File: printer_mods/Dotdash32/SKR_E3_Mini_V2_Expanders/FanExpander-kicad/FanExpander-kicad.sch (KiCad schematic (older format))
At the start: 52 parts, among them J1 FAN1_IN, J10 FAN2, J11 V_SELECT3, J12 V_SELECT4, J13 FAN3, J14 FAN4, J15 V_SELECT5, J16 V_SELECT6, J17 FAN5, J18 FAN6, J2 HV_IN, J3 EXP1_IN, J4 TH2, J5 3V3_IN, J6 V_SELECT1, J7 V_SELECT2, J8 TH2, J9 FAN1, Q1 IRLML6344, Q2 IRLML6344, Q3 IRLML6344, Q4 IRLML6344, Q5 IRLML6344

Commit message: feat: no ADC in EXP1, add more fans!!!
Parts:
- removed C1, C2: 10uF, Capacitors_SMD:C_0805, symbol Device:C
- removed J4, J8: TH2, Connectors_JST:JST_XH_B02B-XH-A_02x2.50mm_Straight, symbol Connector_Generic:Conn_01x02
- removed J5: 3V3_IN, Pin_Headers:Pin_Header_Straight_1x01_Pitch2.54mm, symbol Connector_Generic:Conn_01x01
- removed R1, R4: 4.7k, Resistors_SMD:R_0603_HandSoldering, symbol Device:R_US
- added D? (x2): LED, LEDs:LED_0603_HandSoldering, symbol Device:LED
- added J?: FAN7, Connectors_JST:JST_XH_B02B-XH-A_02x2.50mm_Straight, symbol Connector_Generic:Conn_01x02
- added J?: V_SELECT7, Pin_Headers:Pin_Header_Straight_1x03_Pitch2.54mm, symbol Jumper:Jumper_3_Open
- added J?: FAN6, Connectors_JST:JST_XH_B02B-XH-A_02x2.50mm_Straight, symbol Connector_Generic:Conn_01x02
- added J?: V_SELECT8, Pin_Headers:Pin_Header_Straight_1x03_Pitch2.54mm, symbol Jumper:Jumper_3_Open
- added JP1: FAN_SEL, Jumper:SolderJumper-3_P1.3mm_Open_RoundedPad1.0x1.5mm_NumberLabels, symbol Jumper:SolderJumper_3_Open
- added JP2: LED_ENABLE, symbol Jumper:SolderJumper_2_Bridged
- added Q? (x2): IRLML6344, TO_SOT_Packages_SMD:SOT-23, symbol Device:Q_NMOS_GSD
- added R? (x2): 560R, Resistors_SMD:R_0603_HandSoldering, symbol Device:R_US
- added R? (x2): 100R, Resistors_SMD:R_0603_HandSoldering, symbol Device:R_US
- added R? (x2): 100k, Resistors_SMD:R_0603_HandSoldering, symbol Device:R_US
- J11, J12, J15, J16, J6, J7: symbol Connector_Generic:Conn_01x03 -> Jumper:Jumper_3_Open
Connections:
- net TH2 is gone; now on net FAN3: J3.3 (Pin_3)
- net TH3 is gone; now on net FAN4: J3.5 (Pin_5)
- net +24V: now also J?.3 (B), J?.3 (B)
- net +5V: now also J?.1 (A), J?.1 (A), JP2.1 (A); no longer R13.2, R14.2, R2.2, R3.2, R7.2, R8.2
- net F6V: now also J?.1 (Pin_1), J?.1 (Pin_1), J?.2 (C), J?.2 (C)
- net FAN3: now also R9.2; no longer J3.7 (Pin_7), R9.1
- net FAN4: now also R10.2; no longer J3.2 (Pin_2), R10.1
- net FAN5: now also J3.7 (Pin_7), R15.2; no longer J3.6 (Pin_6), R15.1
- net FAN6: now also J3.2 (Pin_2); no longer J3.8 (Pin_8)
- net GND: now also R10.1, R15.1, R9.1, Q?.2 (S), Q?.2 (S), R?.2, R?.2; no longer R10.2, R15.2, R9.2
- net at J3.4 (Pin_4): now also JP1.3 (B)
- net toFuse24V: no longer names the net of F1.2
- net toFuse24V: no longer J1.1 (Pin_1)
- net toFuse5V: no longer names the net of F3.2
- net toFuse5V: no longer J3.10 (Pin_10)
- new net: J3.8 (Pin_8), JP1.1 (A)
- new net: Q?.1 (G), R?.1 (x2)
- new net: D?.2 (A), R?.1 (x2)
- new net 24V_unFused: J1.1 (Pin_1)
- new net 5V_unFused: J3.10 (Pin_10)
- new net FAN7: J3.6 (Pin_6), R?.1, R?.2
- new net FAN7_Drive: D?.1 (K), J?.2 (Pin_2), Q?.3 (D)
- new net FAN8: JP1.2 (C), R?.1, R?.2
- new net FAN8_Drive: D?.1 (K), J?.2 (Pin_2), Q?.3 (D)
- new net LED_Drive: JP2.2 (B), R13.2, R14.2, R2.2, R3.2, R7.2, R8.2, R?.2, R?.2
- no-connect marks 1 -> 0
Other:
- note added: "FAN1"
- note added: "FAN1 is a pass through fan.\nIt is included for a simple +12/24V reference,\nand to select drive voltage.\n\nNo control is done to this fan!"
- note added: "FAN1\nfrom SKR"
- note added: "Fan2"
- note added: "Fan3"
- note added: "Fan4"
- note added: "Fan5"
- note added: "Fan6"
- note added: "Fan7"
- note added: "Fan8"
- note added: "SKR Mini E3 V2.0\nPB5 | PA15\nTX1/PA9 | RST\nRX1/PA10 | PB9\nPB8 | PB15\nGND | +5V"
- note removed: "3.3V \nfrom SKR"
- note removed: "FAN1 - Passthrough"
- note removed: "FAN1 from SKR"
- note removed: "Fan2 - PB5"
- note removed: "Fan3 - PB8"
- note removed: "Fan4 - PA15"
- note removed: "Fan5 - PB9"
- note removed: "Fan6 - PB15"
- note removed: "PB5 | PA15\nTX1/PA9 | RST\nRX1/PA10 | PB9\nPB8 | PB15\nGND | +5V"
- note removed: "TH2 - PA9"
- note removed: "TH3 - PA10"
- note removed: "Thermistor Inputs"
- moved on the sheet: D3, D4, D5, D6, D7, D8, F1, F3, J1, J10, J13, J14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

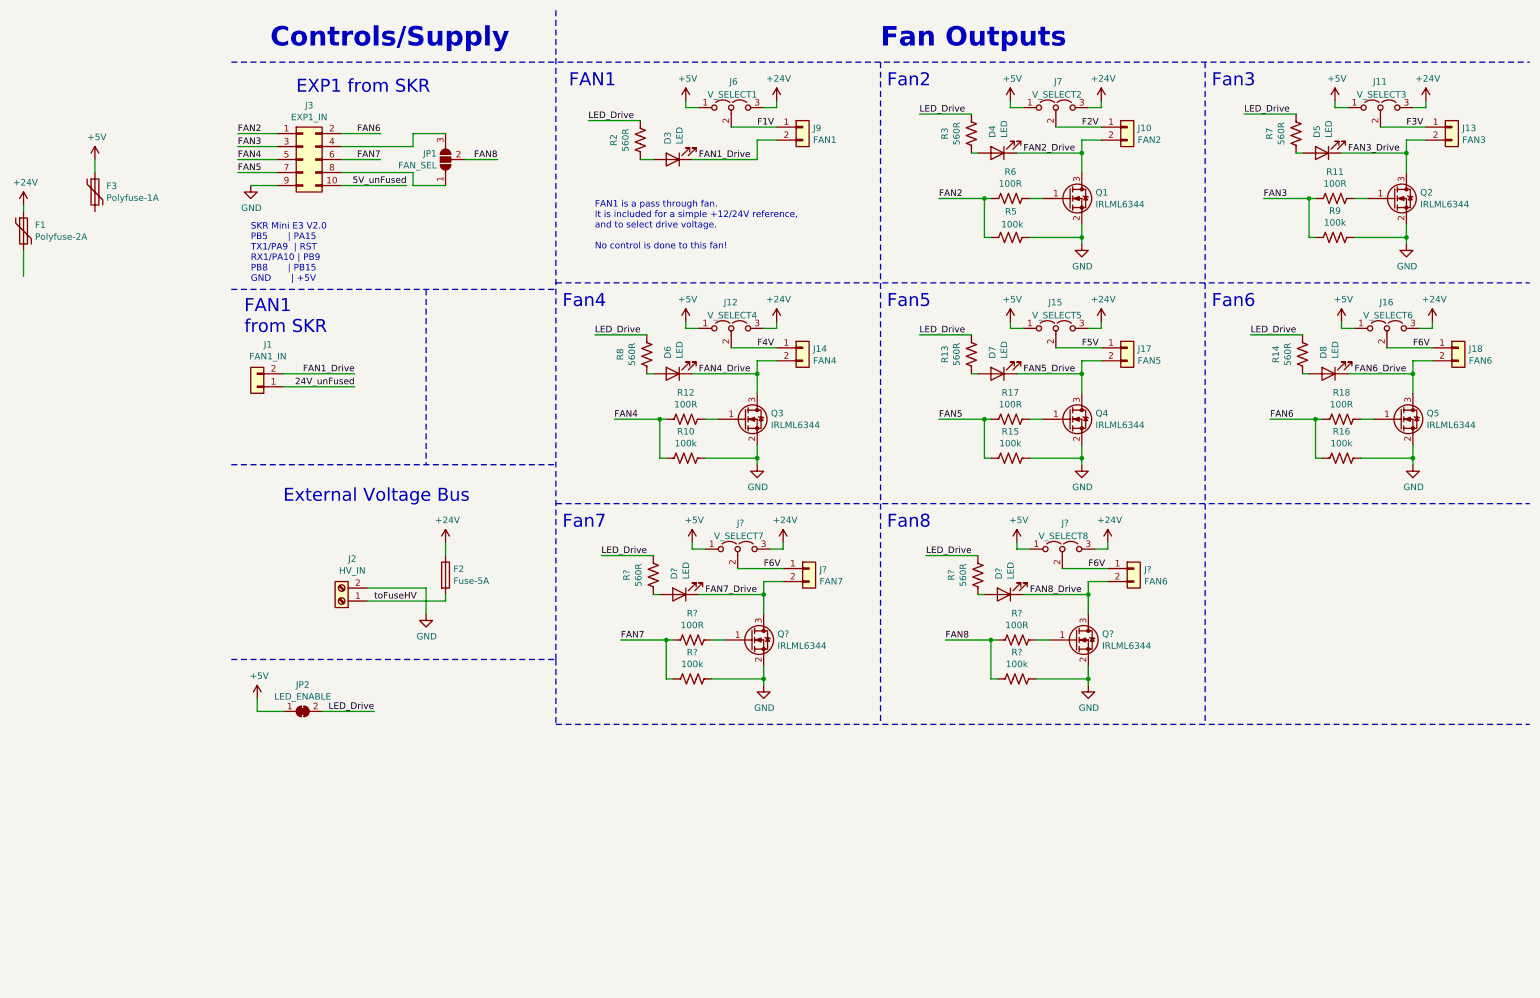
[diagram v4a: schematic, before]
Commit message: feat: beefy expander sch cleaned, initial layout
schematic looks good, but the layout needs work.
RN, it covers too much, so needs to have the EXP header stick out
a lot more than it already is, probably make the whole thing longer
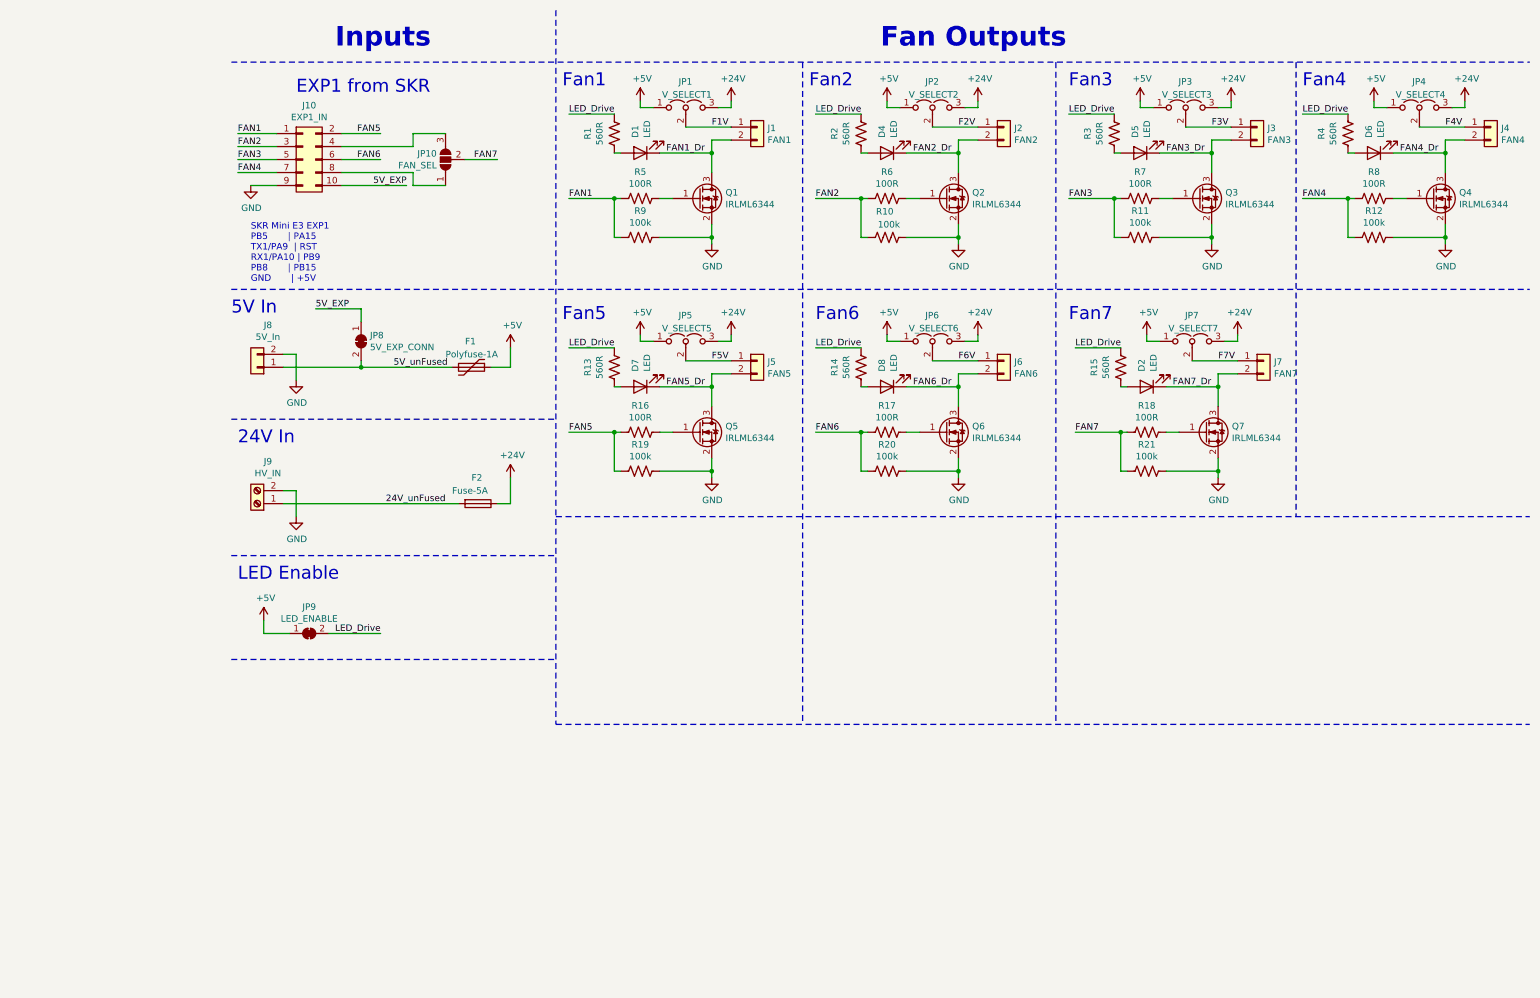
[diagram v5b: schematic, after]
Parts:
- removed D3: LED, LEDs:LED_0603_HandSoldering, symbol Device:LED
- removed F1: Polyfuse-2A, Fuse_Holders_and_Fuses:Fuse_SMD1206_HandSoldering, symbol Device:Polyfuse
- removed J6: V_SELECT1, Pin_Headers:Pin_Header_Straight_1x03_Pitch2.54mm, symbol Jumper:Jumper_3_Open
- removed J9: FAN1, Connectors_JST:JST_XH_B02B-XH-A_02x2.50mm_Straight, symbol Connector_Generic:Conn_01x02
- removed R2: 560R, Resistors_SMD:R_0603_HandSoldering, symbol Device:R_US
- added JP8: 5V_EXP_CONN, Jumper:SolderJumper-2_P1.3mm_Bridged_RoundedPad1.0x1.5mm, symbol Jumper:SolderJumper_2_Bridged
- F2: footprint Fuse_Holders_and_Fuses:BladeFuse-CarType -> Fuse_Holders_and_Fuses:BladeFuse-Mini
- J1: renamed from J?; value FAN6 -> FAN1
- J8: renamed from J1; value FAN1_IN -> 5V_In
- JP1: renamed from J?; value V_SELECT8 -> V_SELECT1
- JP9: renamed from JP2; footprint (none) -> Jumper:SolderJumper-2_P1.3mm_Bridged_RoundedPad1.0x1.5mm
- gave numbers to parts that had none: 12
- renumbered F3 to F1, J3 to J10, J10 to J2, J13 to J3, J14 to J4, J17 to J5, J18 to J6, J2 to J9, JP1 to JP10, J7 to JP2, J11 to JP3, J12 to JP4, J15 to JP5, J16 to JP6, Q1 to Q2, Q2 to Q3, Q3 to Q4, Q4 to Q5, Q5 to Q6, R5 to R10, R9 to R11, R10 to R12, R17 to R16, R18 to R17, R15 to R19, R3 to R2, R16 to R20, R7 to R3, R8 to R4, R11 to R7, R12 to R8
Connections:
- net FAN1_Drive is gone; now on net GND: J8.2 (Pin_2)
- net toFuseHV is gone; now on net 24V_unFused: F2.2, J9.1 (Pin_1)
- net 24V_unFused: no longer J8.1 (Pin_1)
- net 5V_unFused: now also F1.2, J8.1 (Pin_1), JP8.2 (B); no longer J10.10 (Pin_10)
- net F1V: now also J1.1 (Pin_1), JP1.2 (C)
- net F6V: no longer J1.1 (Pin_1), J7.1 (Pin_1), JP1.2 (C), JP7.2 (C)
- net FAN2: now also J10.3 (Pin_3); no longer J10.1 (Pin_1)
- net FAN3: now also J10.5 (Pin_5); no longer J10.3 (Pin_3)
- net FAN4: now also J10.7 (Pin_7); no longer J10.5 (Pin_5)
- net FAN5: now also J10.2 (Pin_2); no longer J10.7 (Pin_7)
- net FAN6: now also J10.6 (Pin_6); no longer J10.2 (Pin_2)
- net FAN7: now also JP10.2 (C); no longer J10.6 (Pin_6)
- net FAN2_Drive renamed FAN2_Dr
- net FAN3_Drive renamed FAN3_Dr
- net FAN4_Drive renamed FAN4_Dr
- net FAN5_Drive renamed FAN5_Dr
- net FAN6_Drive renamed FAN6_Dr
- net FAN7_Drive renamed FAN7_Dr
- net FAN8 renamed FAN1
- net FAN1: now also J10.1 (Pin_1); no longer JP10.2 (C)
- net FAN8_Drive renamed FAN1_Dr
- new net 5V_EXP: J10.10 (Pin_10), JP8.1 (A)
- new net F7V: J7.1 (Pin_1), JP7.2 (C)
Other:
- note added: "24V In"
- note added: "5V In"
- note added: "Fan1"
- note added: "Inputs"
- note added: "LED Enable"
- note added: "SKR Mini E3 EXP1\nPB5 | PA15\nTX1/PA9 | RST\nRX1/PA10 | PB9\nPB8 | PB15\nGND | +5V"
- note removed: "Controls/Supply"
- note removed: "External Voltage Bus"
- note removed: "FAN1"
- note removed: "FAN1 is a pass through fan.\nIt is included for a simple +12/24V reference,\nand to select drive voltage.\n\nNo control is done to this fan!"
- note removed: "FAN1\nfrom SKR"
- note removed: "Fan8"
- note removed: "SKR Mini E3 V2.0\nPB5 | PA15\nTX1/PA9 | RST\nRX1/PA10 | PB9\nPB8 | PB15\nGND | +5V"
- moved on the sheet: D1, D2, D4, D5, D6, D7, D8, F1, F2, J1, J2, J3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

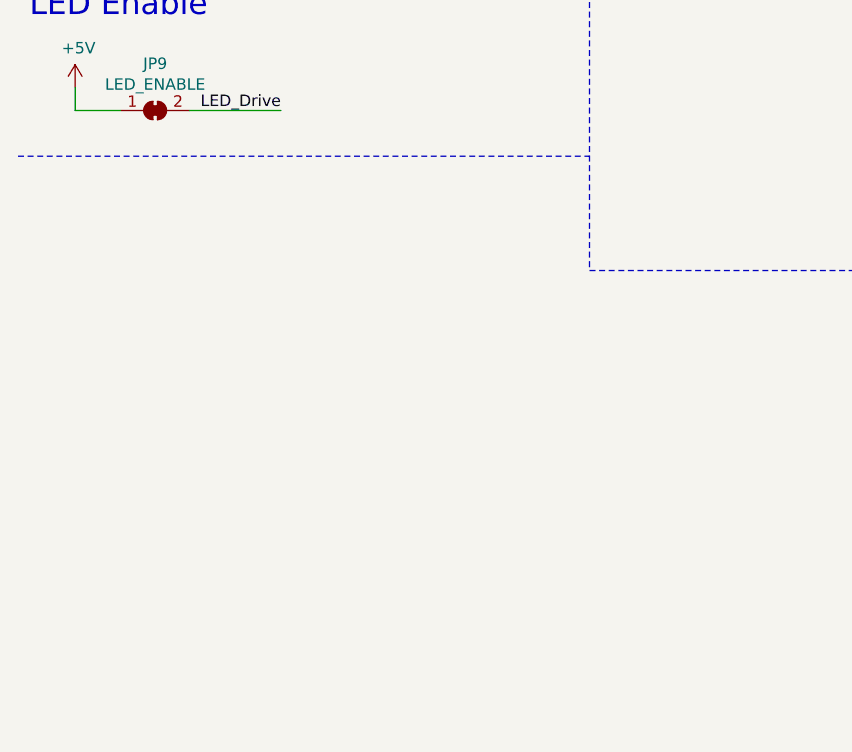
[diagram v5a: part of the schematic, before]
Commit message: test: using 1xXX pins for breakaways?
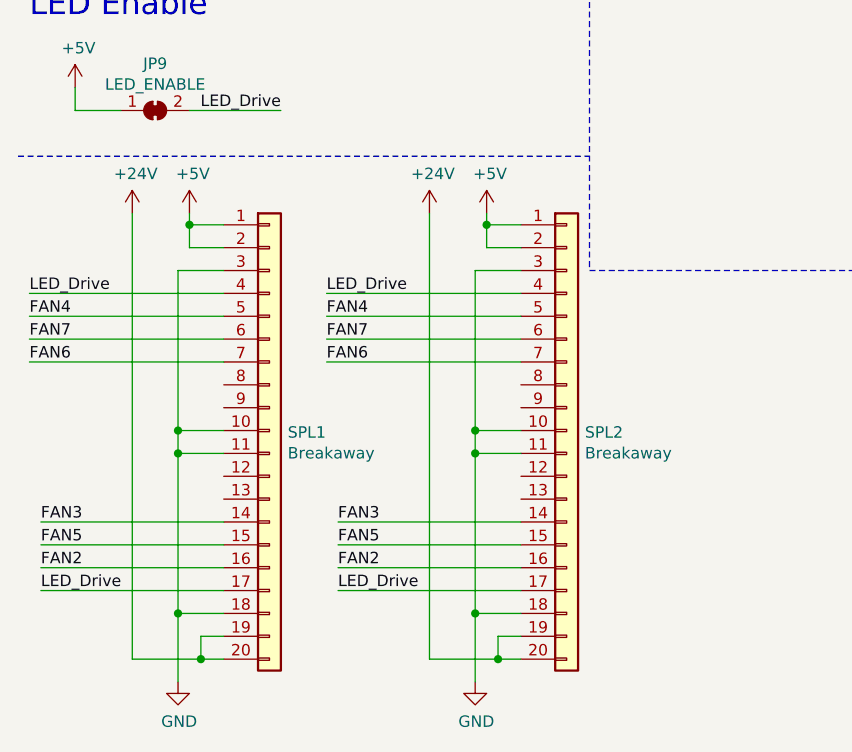
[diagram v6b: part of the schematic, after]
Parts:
- added SPL1, SPL2: Breakaway, Pin_Headers:Pin_Header_Straight_1x20_Pitch1.00mm, symbol Connector_Generic:Conn_01x20
- F1: footprint Fuse_Holders_and_Fuses:Fuse_SMD1206_HandSoldering -> Fuse_Holders_and_Fuses:Fuse_SMD1206_Reflow
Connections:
- net +24V: now also SPL1.19 (Pin_19), SPL1.20 (Pin_20), SPL2.19 (Pin_19), SPL2.20 (Pin_20)
- net +5V: now also SPL1.1 (Pin_1), SPL1.2 (Pin_2), SPL2.1 (Pin_1), SPL2.2 (Pin_2)
- net FAN2: now also SPL1.16 (Pin_16), SPL2.16 (Pin_16)
- net FAN3: now also SPL1.14 (Pin_14), SPL2.14 (Pin_14)
- net FAN4: now also SPL1.5 (Pin_5), SPL2.5 (Pin_5)
- net FAN5: now also SPL1.15 (Pin_15), SPL2.15 (Pin_15)
- net FAN6: now also SPL1.7 (Pin_7), SPL2.7 (Pin_7)
- net FAN7: now also SPL1.6 (Pin_6), SPL2.6 (Pin_6)
- net GND: now also SPL1.10 (Pin_10), SPL1.11 (Pin_11), SPL1.18 (Pin_18), SPL1.3 (Pin_3), SPL2.10 (Pin_10), SPL2.11 (Pin_11), SPL2.18 (Pin_18), SPL2.3 (Pin_3)
- net LED_Drive: now also SPL1.17 (Pin_17), SPL1.4 (Pin_4), SPL2.17 (Pin_17), SPL2.4 (Pin_4)
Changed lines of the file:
@@
 F 0 "F1" V 2150 3200 50  0000 L CNN
 F 1 "Polyfuse-1A" V 2250 3050 50  0000 L CNN
-F 2 "Fuse_Holders_and_Fuses:Fuse_SMD1206_HandSoldering" H 2400 3050 50  0001 L CNN
+F 2 "Fuse_Holders_and_Fuses:Fuse_SMD1206_Reflow" H 2400 3050 50  0001 L CNN
 F 3 "~" H 2350 3250 50  0001 C CNN
 	1    2350 3250
@@
 Text Notes 550  4900 0    100  ~ 0
 LED Enable
-Wire Notes Line
-	500  5500 3000 5500
 Wire Notes Line width 12 style solid
 	3000 500  3000 6000
@@
 Wire Wire Line
 	1500 3250 2200 3250
+$Comp
+L power:GND #PWR0103
+U 1 1 61E47425
+P 1200 7800
+F 0 "#PWR0103" H 1200 7550 50  0001 C CNN
+F 1 "GND" H 1205 7627 50  0000 C CNN
+F 2 "" H 1200 7800 50  0001 C CNN
+F 3 "" H 1200 7800 50  0001 C CNN
+	1    1200 7800
+	1    0    0    -1
+$EndComp
+$Comp
+L Connector_Generic:Conn_01x20 SPL1
+U 1 1 61ED7192
+P 1600 6700
+F 0 "SPL1" H 1680 6692 50  0000 L CNN
+F 1 "Breakaway" H 1680 6601 50  0000 L CNN
+F 2 "Pin_Headers:Pin_Header_Straight_1x20_Pitch1.00mm" H 1600 6700 50  0001 C CNN
+F 3 "~" H 1600 6700 50  0001 C CNN
+	1    1600 6700
+	1    0    0    -1
+$EndComp
+$Comp
+L power:+24V #PWR0105
+U 1 1 61EDE44B
+P 1000 5750
+F 0 "#PWR0105" H 1000 5600 50  0001 C CNN
+F 1 "+24V" H 1015 5923 50  0000 C CNN
+F 2 "" H 1000 5750 50  0001 C CNN
+F 3 "" H 1000 5750 50  0001 C CNN
+	1    1000 5750
+	1    0    0    -1
+$EndComp
+$Comp
+L power:+5V #PWR0106
+U 1 1 61EDCDF9
+P 1250 5750
+F 0 "#PWR0106" H 1250 5600 50  0001 C CNN
+F 1 "+5V" H 1265 5923 50  0000 C CNN
+F 2 "" H 1250 5750 50  0001 C CNN
+F 3 "" H 1250 5750 50  0001 C CNN
+	1    1250 5750
+	1    0    0    -1
+$EndComp
+Wire Wire Line
+	1250 5750 1250 5800
+Wire Wire Line
+	1250 5800 1400 5800
+Wire Wire Line
+	1400 5900 1250 5900
+Wire Wire Line
+	1250 5900 1250 5800
+Connection ~ 1250 5800
+Wire Wire Line
+	1000 5750 1000 7700
+Wire Wire Line
+	1000 7700 1300 7700
+Wire Wire Line
+	1400 7600 1300 7600
+Wire Wire Line
+	1300 7600 1300 7700
+Connection ~ 1300 7700
+Wire Wire Line
+	1300 7700 1400 7700
+Wire Wire Line
+	1200 7800 1200 7500
+Wire Wire Line
+	1200 7500 1400 7500
+Wire Wire Line
+	1200 7500 1200 6800
+Wire Wire Line
+	1200 6000 1400 6000
+Connection ~ 1200 7500
+Wire Wire Line
+	1400 6100 550  6100
+Text Label 550  6100 0    50   ~ 0
+LED_Drive
+Wire Wire Line
+	1400 6700 1200 6700
+Connection ~ 1200 6700
+Wire Wire Line
+	1200 6700 1200 6000
+Wire Wire Line
+	1400 6800 1200 6800
+Connection ~ 1200 6800
+Wire Wire Line
+	1200 6800 1200 6700
+Wire Wire Line
+	1400 6200 550  6200
+Wire Wire Line
+	1400 6300 550  6300
+Wire Wire Line
+	1400 6400 550  6400
+Wire Wire Line
+	1400 7400 600  7400
+Wire Wire Line
+	1400 7300 600  7300
+Wire Wire Line
+	1400 7200 600  7200
+Wire Wire Line
+	1400 7100 600  7100
+Text Label 600  7300 0    50   ~ 0
+FAN2
+Text Label 600  7200 0    50   ~ 0
+FAN5
+Text Label 550  6200 0    50   ~ 0
+FAN4
+Text Label 550  6300 0    50   ~ 0
+FAN7
+Text Label 600  7100 0    50   ~ 0
+FAN3
+Text Label 550  6400 0    50   ~ 0
+FAN6
+Text Label 600  7400 0    50   ~ 0
+LED_Drive
+$Comp
+L power:GND #PWR0107
+U 1 1 61FFF90D
+P 2500 7800
+F 0 "#PWR0107" H 2500 7550 50  0001 C CNN
+F 1 "GND" H 2505 7627 50  0000 C CNN
+F 2 "" H 2500 7800 50  0001 C CNN
+F 3 "" H 2500 7800 50  0001 C CNN
+	1    2500 7800
+	1    0    0    -1
+$EndComp
+$Comp
+L Connector_Generic:Conn_01x20 SPL2
+U 1 1 61FFF913
+P 2900 6700
+F 0 "SPL2" H 2980 6692 50  0000 L CNN
+F 1 "Breakaway" H 2980 6601 50  0000 L CNN
+F 2 "Pin_Headers:Pin_Header_Straight_1x20_Pitch1.00mm" H 2900 6700 50  0001 C CNN
+F 3 "~" H 2900 6700 50  0001 C CNN
+	1    2900 6700
+	1    0    0    -1
+$EndComp
+$Comp
+L power:+24V #PWR0108
+U 1 1 61FFF919
+P 2300 5750
+F 0 "#PWR0108" H 2300 5600 50  0001 C CNN
+F 1 "+24V" H 2315 5923 50  0000 C CNN
+F 2 "" H 2300 5750 50  0001 C CNN
+F 3 "" H 2300 5750 50  0001 C CNN
+	1    2300 5750
+	1    0    0    -1
+$EndComp
+$Comp
+L power:+5V #PWR0109
+U 1 1 61FFF91F
+P 2550 5750
+F 0 "#PWR0109" H 2550 5600 50  0001 C CNN
+F 1 "+5V" H 2565 5923 50  0000 C CNN
+F 2 "" H 2550 5750 50  0001 C CNN
+F 3 "" H 2550 5750 50  0001 C CNN
+	1    2550 5750
+	1    0    0    -1
+$EndComp
+Wire Wire Line
+	2550 5750 2550 5800
+Wire Wire Line
+	2550 5800 2700 5800
+Wire Wire Line
+	2700 5900 2550 5900
+Wire Wire Line
+	2550 5900 2550 5800
+Connection ~ 2550 5800
+Wire Wire Line
+	2300 5750 2300 7700
+Wire Wire Line
+	2300 7700 2600 7700
+Wire Wire Line
+	2700 7600 2600 7600
+Wire Wire Line
+	2600 7600 2600 7700
+Connection ~ 2600 7700
+Wire Wire Line
+	2600 7700 2700 7700
+Wire Wire Line
+	2500 7800 2500 7500
+Wire Wire Line
+	2500 7500 2700 7500
+Wire Wire Line
+	2500 7500 2500 6800
+Wire Wire Line
+	2500 6000 2700 6000
+Connection ~ 2500 7500
+Wire Wire Line
+	2700 6100 1850 6100
+Text Label 1850 6100 0    50   ~ 0
+LED_Drive
+Wire Wire Line
+	2700 6700 2500 6700
+Connection ~ 2500 6700
+Wire Wire Line
+	2500 6700 2500 6000
+Wire Wire Line
+	2700 6800 2500 6800
+Connection ~ 2500 6800
+Wire Wire Line
+	2500 6800 2500 6700
+Wire Wire Line
+	2700 6200 1850 6200
+Wire Wire Line
+	2700 6300 1850 6300
+Wire Wire Line
+	2700 6400 1850 6400
+Wire Wire Line
+	2700 7400 1900 7400
+Wire Wire Line
+	2700 7300 1900 7300
+Wire Wire Line
+	2700 7200 1900 7200
+Wire Wire Line
+	2700 7100 1900 7100
+Text Label 1900 7300 0    50   ~ 0
+FAN2
+Text Label 1900 7200 0    50   ~ 0
+FAN5
+Text Label 1850 6200 0    50   ~ 0
+FAN4
+Text Label 1850 6300 0    50   ~ 0
+FAN7
+Text Label 1900 7100 0    50   ~ 0
+FAN3
+Text Label 1850 6400 0    50   ~ 0
+FAN6
+Text Label 1900 7400 0    50   ~ 0
+LED_Drive
+Wire Notes Line
+	500  5500 3000 5500
 $EndSCHEMATC
